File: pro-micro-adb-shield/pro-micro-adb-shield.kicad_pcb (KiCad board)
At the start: 2 copper layers, 18 x 44 mm, 9 parts, among them J1 Mini-DIN-4, SW1 SW_Push_Dual, SW2 SW_DIP_x04, U1 Arduino_Pro_Micro

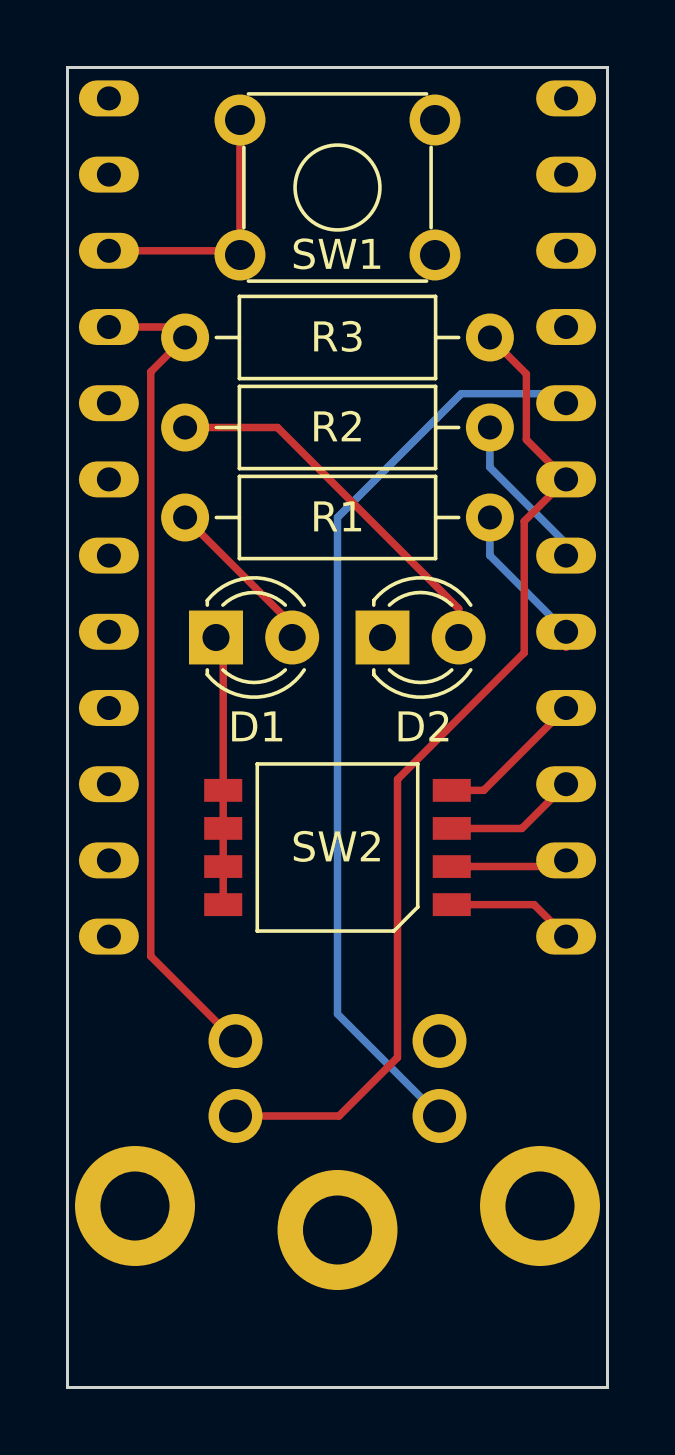
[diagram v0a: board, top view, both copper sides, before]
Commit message: Add 3D model for switch, setup OSHPark constraints
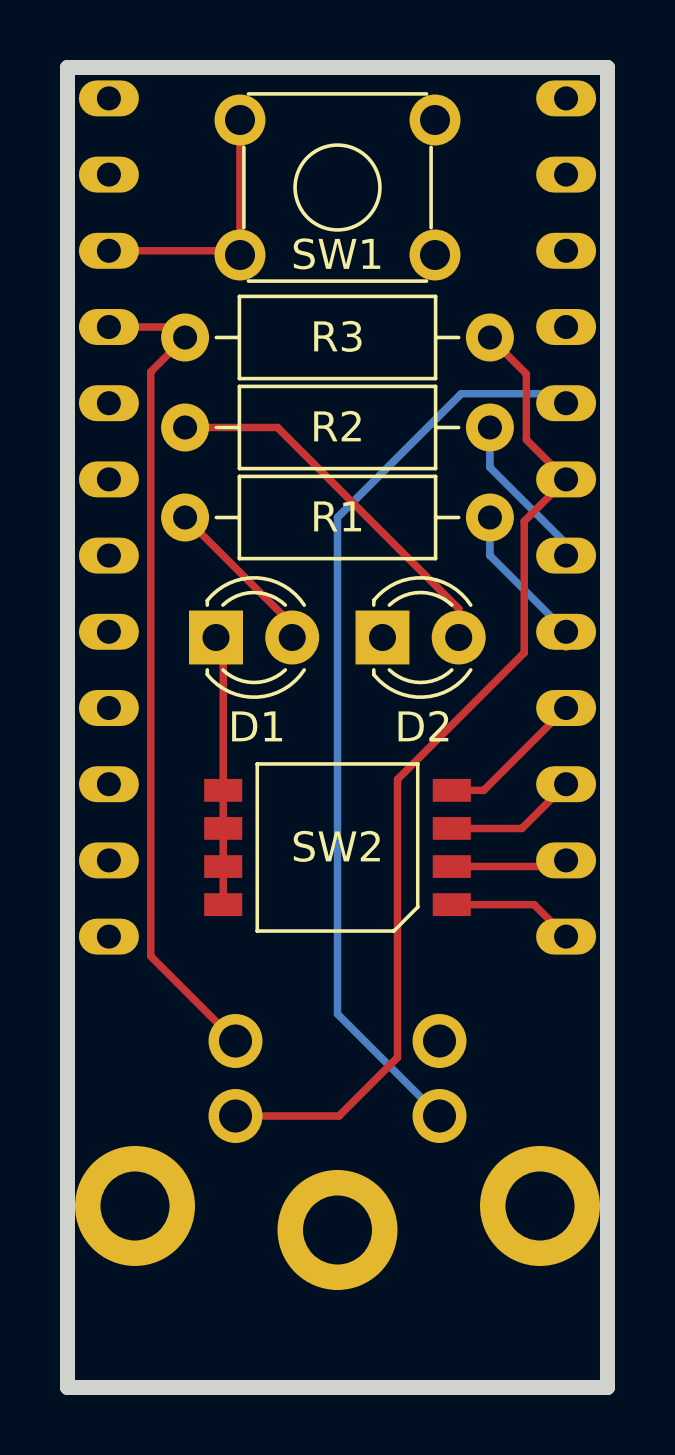
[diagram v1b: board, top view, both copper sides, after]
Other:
- outline, holes or cut-outs redrawn
- rule pad_to_mask_clearance: 0 -> 0.0508
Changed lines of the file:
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@@
   )
   (setup
-    (pad_to_mask_clearance 0)
+    (stackup
+      (layer "F.SilkS" (type "Top Silk Screen"))
+      (layer "F.Paste" (type "Top Solder Paste"))
+      (layer "F.Mask" (type "Top Solder Mask") (color "Green") (thickness 0.01))
+      (layer "F.Cu" (type "copper") (thickness 0.035))
+      (layer "dielectric 1" (type "core") (thickness 1.51) (material "FR4") (epsilon_r 4.5) (loss_tangent 0.02))
+      (layer "B.Cu" (type "copper") (thickness 0.035))
+      (layer "B.Mask" (type "Bottom Solder Mask") (color "Green") (thickness 0.01))
+      (layer "B.Paste" (type "Bottom Solder Paste"))
+      (layer "B.SilkS" (type "Bottom Silk Screen"))
+      (copper_finish "None")
+      (dielectric_constraints no)
+    )
+    (pad_to_mask_clearance 0.0508)
+    (aux_axis_origin 99 112)
+    (grid_origin 99 112)
     (pcbplotparams
       (layerselection 0x00010fc_ffffffff)
@@
       (outputformat 1)
       (mirror false)
-      (drillshape 1)
+      (drillshape 0)
       (scaleselection 1)
-      (outputdirectory "")
+      (outputdirectory "../manufacturing/")
     )
   )
@@
       (rotate (xyz 0 0 0))
     )
+    (model "/home/cnorthway/repos/pro_micro_adb_shield/personal-kicad-lib/3d/c-1825910-7-c-3d.stp"
+      (offset (xyz 3.25 -2.25 5.25))
+      (scale (xyz 1 1 1))
+      (rotate (xyz 0 0 90))
+    )
   )
   (footprint "cnorthway:218-4LPST" (layer "F.Cu")
@@
     (fp_line (start -2.54 4.7) (end -2.54 -4.7) (layer "F.CrtYd") (width 0.05))
     (pad "1" smd rect (at -1.905 3.81 90) (size 0.76 1.27) (layers "F.Cu" "F.Paste" "F.Mask")
-      (net 15 "DIP4") (pintype "passive"))
+      (net 15 "DIP4"))
     (pad "2" smd rect (at -0.635 3.81 90) (size 0.76 1.27) (layers "F.Cu" "F.Paste" "F.Mask")
-      (net 14 "DIP3") (pintype "passive"))
+      (net 14 "DIP3"))
     (pad "3" smd rect (at 0.635 3.81 90) (size 0.76 1.27) (layers "F.Cu" "F.Paste" "F.Mask")
-      (net 10 "DIP2") (pintype "passive"))
+      (net 10 "DIP2"))
     (pad "4" smd rect (at 1.905 3.81 90) (size 0.76 1.27) (layers "F.Cu" "F.Paste" "F.Mask")
-      (net 4 "DIP1") (pintype "passive"))
+      (net 4 "DIP1"))
     (pad "5" smd rect (at 1.905 -3.81 90) (size 0.76 1.27) (layers "F.Cu" "F.Paste" "F.Mask")
-      (net 1 "GND") (pintype "passive"))
+      (net 1 "GND"))
     (pad "6" smd rect (at 0.635 -3.81 90) (size 0.76 1.27) (layers "F.Cu" "F.Paste" "F.Mask")
-      (net 1 "GND") (pintype "passive"))
+      (net 1 "GND"))
     (pad "7" smd rect (at -0.635 -3.81 90) (size 0.76 1.27) (layers "F.Cu" "F.Paste" "F.Mask")
-      (net 1 "GND") (pintype "passive"))
+      (net 1 "GND"))
     (pad "8" smd rect (at -1.905 -3.81 90) (size 0.76 1.27) (layers "F.Cu" "F.Paste" "F.Mask")
-      (net 1 "GND") (pintype "passive"))
+      (net 1 "GND"))
     (model "${KIPRJMOD}/../personal-kicad-lib/3d/218-4.STEP"
       (offset (xyz 0 0 0.75))
@@
       (net 24 "unconnected-(U1-Pad24)") (pinfunction "RAW") (pintype "power_in+no_connect"))
   )
-  (gr_line (start 99 98) (end 99 112) (layer "Edge.Cuts") (width 0.1))
-  (gr_line (start 99 68) (end 99 98) (layer "Edge.Cuts") (width 0.1))
-  (gr_line (start 117 68) (end 99 68) (layer "Edge.Cuts") (width 0.1))
-  (gr_line (start 99 112) (end 117 112) (layer "Edge.Cuts") (width 0.1))
-  (gr_line (start 117 112) (end 117 68) (layer "Edge.Cuts") (width 0.1))
+  (gr_line (start 99 68) (end 99 112) (layer "Edge.Cuts") (width 0.5))
+  (gr_line (start 117 68) (end 99 68) (layer "Edge.Cuts") (width 0.5))
+  (gr_line (start 99 112) (end 117 112) (layer "Edge.Cuts") (width 0.5))
+  (gr_line (start 117 112) (end 117 68) (layer "Edge.Cuts") (width 0.5))
   (segment (start 104.19 95.905) (end 104.19 87.24) (width 0.25) (layer "F.Cu") (net 1))
   (segment (start 104.19 87.24) (end 103.95 87) (width 0.25) (layer "F.Cu") (net 1))

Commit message: Modify edge cut, add silkscreen
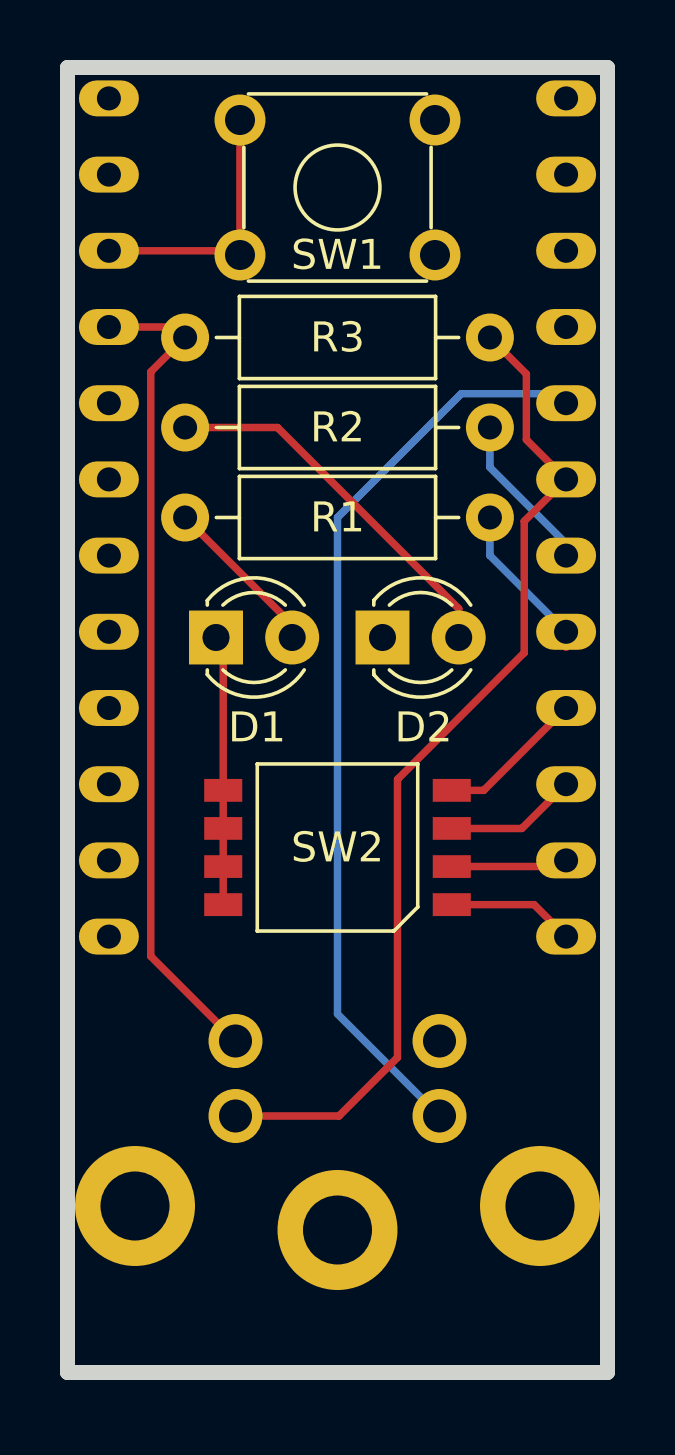
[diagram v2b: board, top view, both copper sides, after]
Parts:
- added REF**: OSHW-Logo2_7.3x6mm_SilkScreen, Symbol:OSHW-Logo2_7.3x6mm_SilkScreen, B.Cu at (108.0, 79.0)
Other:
- board size 18 x 44 mm -> 18 x 43.5 mm
- board text added: "Pro Micro ADB-USB Converter Connor Northway"

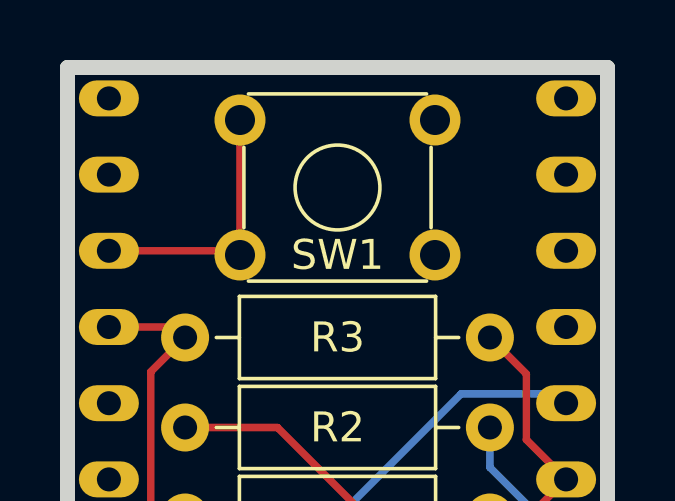
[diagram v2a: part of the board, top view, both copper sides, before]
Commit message: Fix shorted RST/GND through button
why does this sort of thing always show up the day after you
send the gerbers in to be manufactured >:(
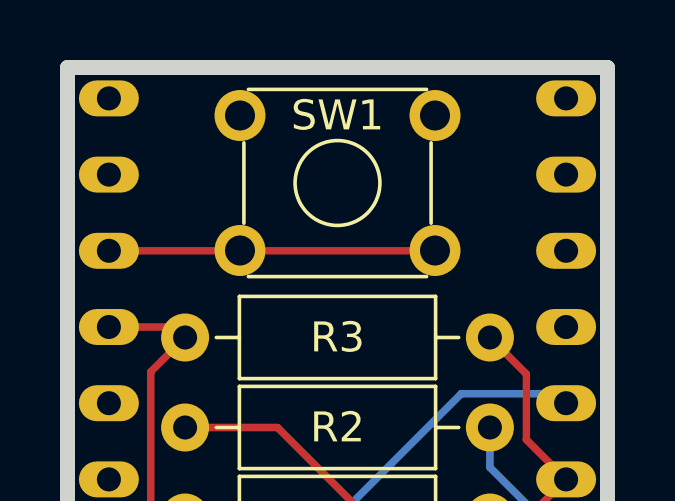
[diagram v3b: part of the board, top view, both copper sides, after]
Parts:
- SW1: value SW_Push_Dual -> SW_Push_Dual_Other_PinLayout
- moved SW1 7.82 mm to (111.2, 74.1), turned to 180 degrees
- moved REF** 0.25 mm to (108.0, 79.2)
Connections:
- SW1 pad 2: GND -> RST
- SW1 pad 3: RST -> GND
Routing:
- net RST: track 8.93 -> 10.9 mm

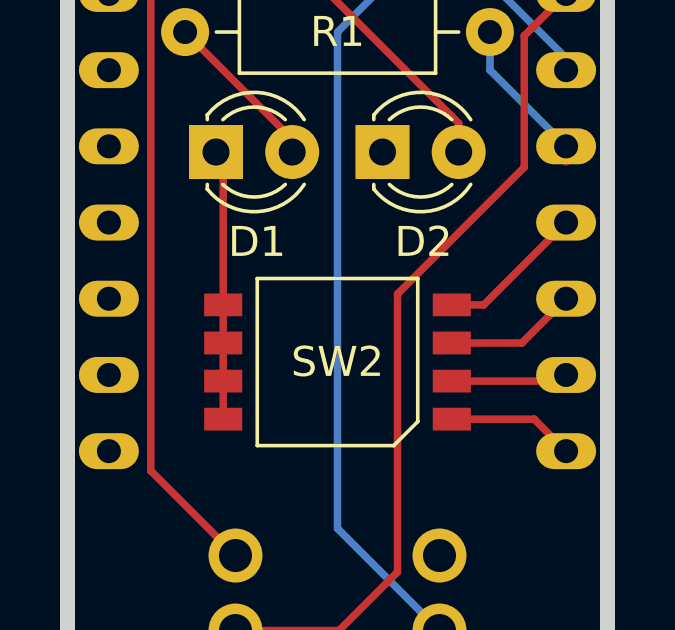
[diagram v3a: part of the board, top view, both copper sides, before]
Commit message: Use env var for 3d models, flip net names for DIP
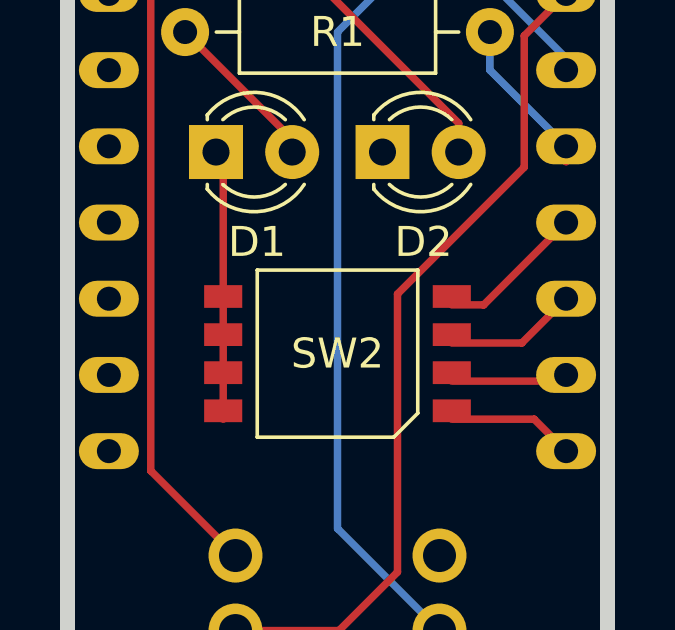
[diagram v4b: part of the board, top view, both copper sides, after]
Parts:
- moved SW2 0.28 mm to (108.0, 93.7)
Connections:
- SW2 pad 1: DIP4 -> DIP1
- SW2 pad 2: DIP3 -> DIP2
- SW2 pad 3: DIP2 -> DIP3
- SW2 pad 4: DIP1 -> DIP4
- U1 pad 10: DIP2 -> DIP3
- U1 pad 11: DIP3 -> DIP2
- U1 pad 12: DIP4 -> DIP1
- U1 pad 9: DIP1 -> DIP4
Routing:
- net DIP4: track 4.25 -> 4.95 mm
- net DIP1: track 4.95 -> 4.25 mm
- net DIP3: track 3.89 -> 4.42 mm
- net DIP2: track 4.42 -> 3.89 mm
